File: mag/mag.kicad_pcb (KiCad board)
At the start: 2 copper layers, 96 x 41 mm, 28 parts, among them K1 кнопка_FSMSM, K2 кнопка_FSMSM

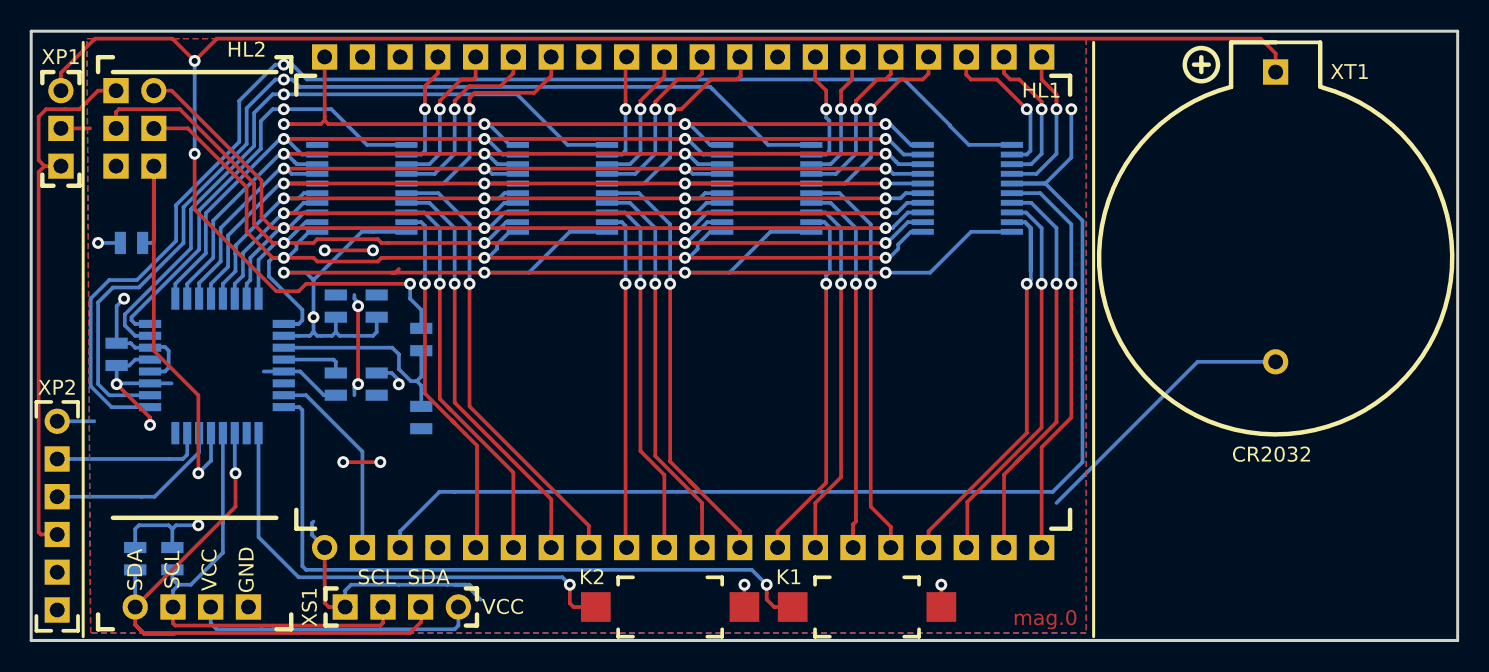
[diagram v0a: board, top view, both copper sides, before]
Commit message: подготавливается переделка под стационарные датчики
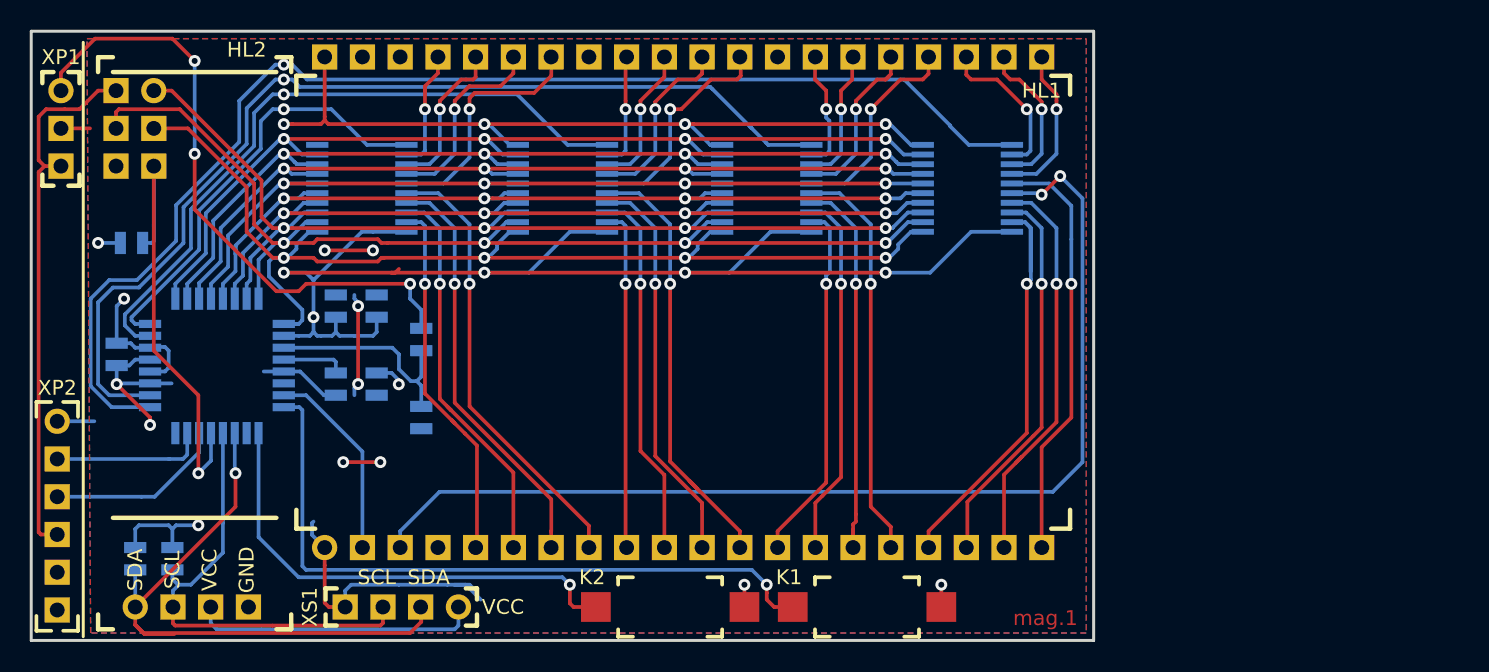
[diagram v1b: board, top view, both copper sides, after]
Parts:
- removed the G*** at (177.8, 61.0)
- removed the G*** at (188.2, 60.0)
- removed XТ1: Клеммник_х2, N_X:батарейный_отсек_CR2032
- added G***: LOGO, N_ICO:instagram_3x3, B.Cu at (120.0, 30.0)
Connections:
- net /PC3 renamed Net-(DD1-Pad26)
- HL1 pad 20: /Out44 -> /Out45
- HL1 pad 3: /Out45 -> /Out44
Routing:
- net /VCC_bat: track 117.1 -> 42.1 mm
- net /Out45: track 79.2 -> 28.4 mm
- net /Out44: track 27.7 -> 72.6 mm, vias 1 -> 2
- net /GND: track 127.7 -> 109.0 mm
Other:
- board size 96 x 41 mm -> 71.5 x 41 mm
- board text added: "el.a.nikitos"
- board text added: "mag.1"
- board text removed: "CR2032"
- board text removed: "mag.0"

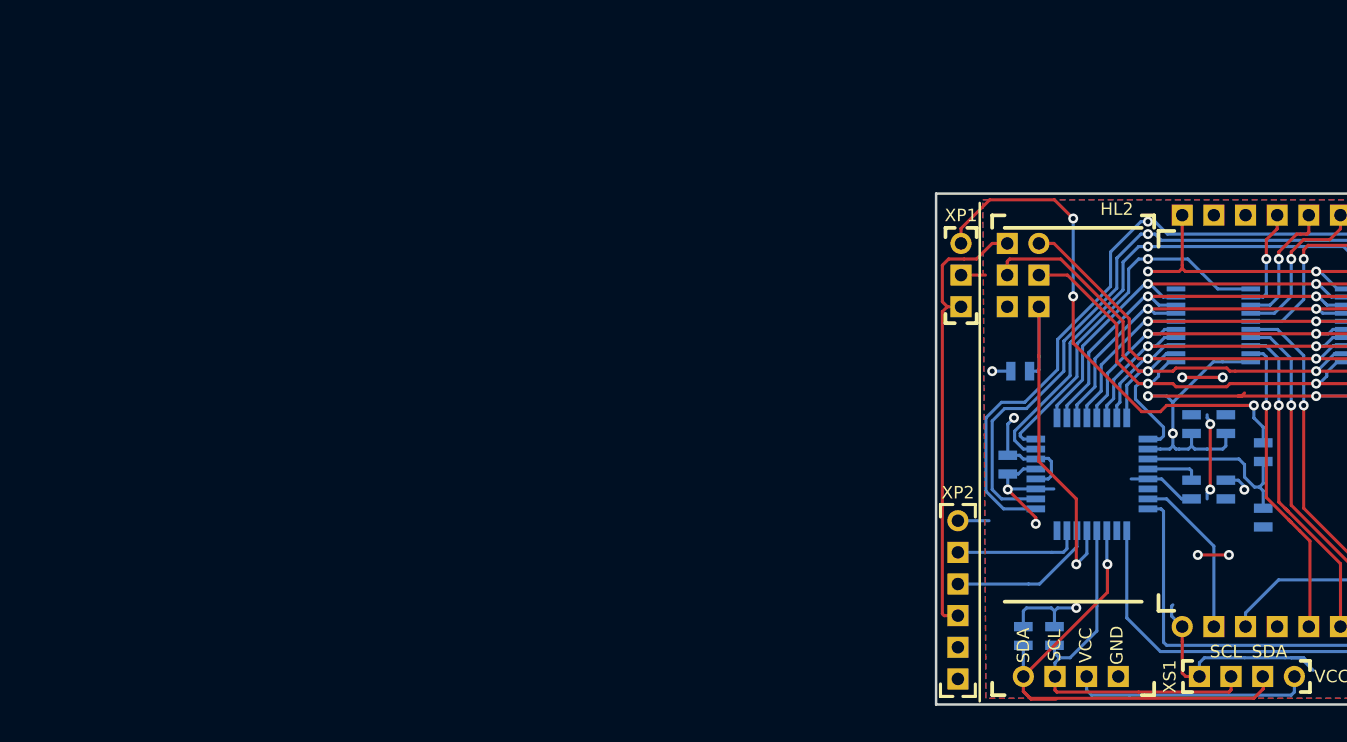
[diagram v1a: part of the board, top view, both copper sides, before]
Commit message: выложена схема питания и преобразователя
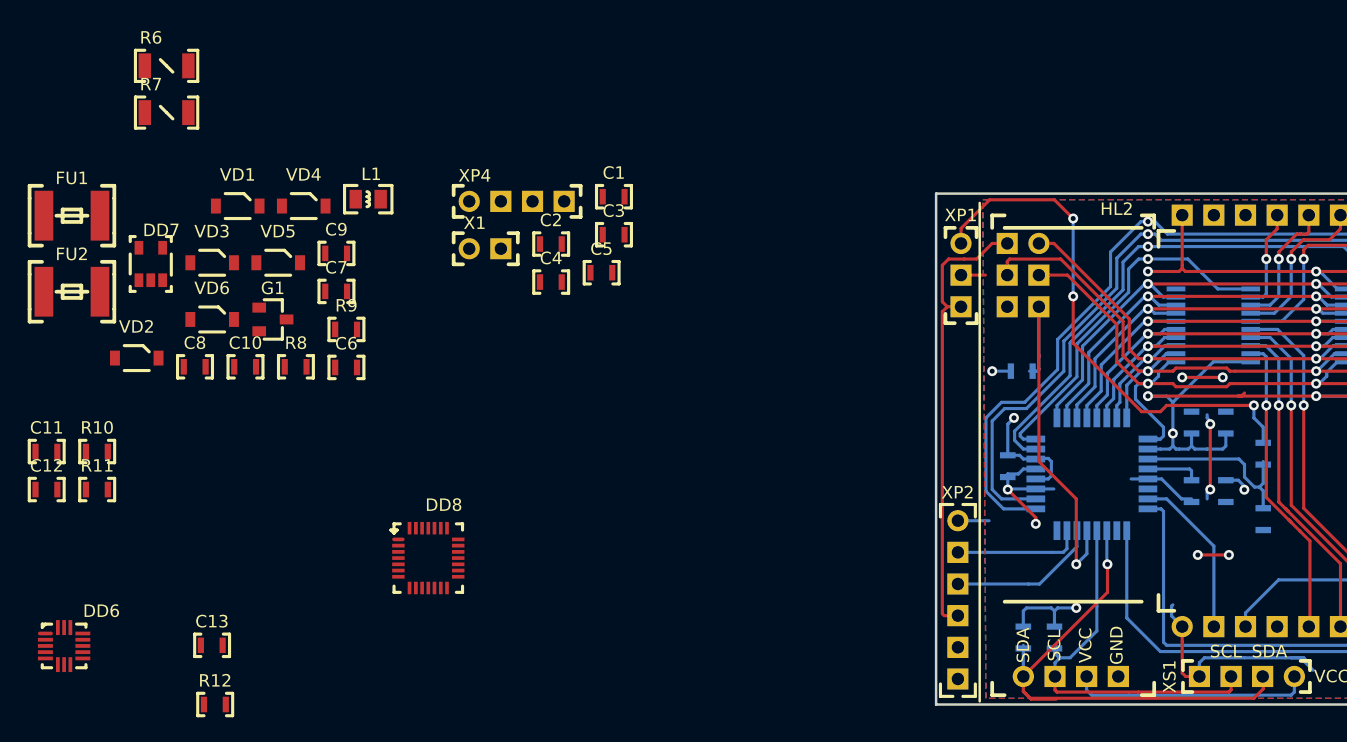
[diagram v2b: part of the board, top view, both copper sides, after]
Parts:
- added C1: Конденсатор_керамический, N_RLC:Конденсатор_SMD_0603, F.Cu at (71.2, 40.5)
- added C10: Конденсатор_керамический, N_RLC:Конденсатор_SMD_0603, F.Cu at (41.7, 54.1)
- added C11: Конденсатор_керамический, N_RLC:Конденсатор_SMD_0603, F.Cu at (25.7, 61.0)
- added C12: Конденсатор_керамический, N_RLC:Конденсатор_SMD_0603, F.Cu at (25.7, 64.0)
- added C13: Конденсатор_керамический, N_RLC:Конденсатор_SMD_0603, F.Cu at (39.0, 76.5)
- added C2: Конденсатор_керамический, N_RLC:Конденсатор_SMD_0603, F.Cu at (66.2, 44.3)
- added C3: Конденсатор_керамический, N_RLC:Конденсатор_SMD_0603, F.Cu at (71.2, 43.5)
- added C4: Конденсатор_керамический, N_RLC:Конденсатор_SMD_0603, F.Cu at (66.2, 47.4)
- added C5: Конденсатор_керамический, N_RLC:Конденсатор_SMD_0603, F.Cu at (70.3, 46.6)
- added C6: Конденсатор_керамический, N_RLC:Конденсатор_SMD_0603, F.Cu at (49.8, 54.2)
- added C7: Конденсатор_керамический, N_RLC:Конденсатор_SMD_0603, F.Cu at (49.0, 48.1)
- added C8: Конденсатор_керамический, N_RLC:Конденсатор_SMD_0603, F.Cu at (37.6, 54.1)
- added C9: Конденсатор_керамический, N_RLC:Конденсатор_SMD_0603, F.Cu at (49.0, 45.0)
- added DD6: LIS3DH, N_DD:акселерометр_LIS3DH, F.Cu at (28.0, 76.5)
- added DD7: Микросхема_DCDC_step_UP_TPS61040, N_G:Преобразователь_LM2703_SOT-23-5, F.Cu at (34.0, 47.2)
- added DD8: Преобразователь_CP2102(USB-UART), N_DD:Микросхема_CP2102, F.Cu at (54.8, 67.0)
- added FU1: Предохранитель_MF-MSMF010, N_RLC:Предохранитель_SMD_1812, F.Cu at (26.4, 42.0)
- added FU2: Предохранитель_MF-MSMF010, N_RLC:Предохранитель_SMD_1812, F.Cu at (26.4, 48.1)
- added G1: стабилизатор_XC6206P302MR, N_VD_HL:Транзистор_IRLML6344TR_SOT-23, F.Cu at (44.8, 50.4)
- added L1: Чип-индуктивность, N_RLC:Чип-индуктивность_SMD_0805, F.Cu at (51.4, 40.7)
- added R10: Резистор_0,065Вт, N_RLC:Конденсатор_SMD_0603, F.Cu at (29.8, 61.0)
- added R11: Резистор_0,065Вт, N_RLC:Конденсатор_SMD_0603, F.Cu at (29.8, 64.0)
- added R12: Резистор_0,065Вт, N_RLC:Конденсатор_SMD_0603, F.Cu at (39.2, 81.2)
- added R6: Резистор_0,25Вт, N_RLC:Резистор_SMD_1206-0,25_Вт, F.Cu at (34.5, 30.0)
- added R7: Резистор_0,25Вт, N_RLC:Резистор_SMD_1206-0,25_Вт, F.Cu at (34.5, 33.8)
- added R8: Резистор_0,065Вт, N_RLC:Конденсатор_SMD_0603, F.Cu at (45.7, 54.1)
- added R9: Резистор_0,065Вт, N_RLC:Конденсатор_SMD_0603, F.Cu at (49.8, 51.1)
- added VD1: Диод_S13, N_VD_HL:Диод_S13_SOD-123, F.Cu at (42.0, 41.2)
- added VD2: Диод_S13, N_VD_HL:Диод_S13_SOD-123, F.Cu at (33.9, 53.5)
- added VD3: Диод_S13, N_VD_HL:Диод_S13_SOD-123, F.Cu at (39.9, 45.8)
- added VD4: Диод_S13, N_VD_HL:Диод_S13_SOD-123, F.Cu at (47.3, 41.2)
- added VD5: Диод_S13, N_VD_HL:Диод_S13_SOD-123, F.Cu at (45.2, 45.8)
- added VD6: Диод_S13, N_VD_HL:Диод_S13_SOD-123, F.Cu at (39.9, 50.4)
- added X1: Клеммник_х2, N_X:Вилка_PLS2_вертикальная, F.Cu at (60.5, 44.7)
- added XP4: USB_female, N_X:Вилка_PLS4_вертикальная, F.Cu at (60.5, 40.9)
- DD1: value ATmega8A-AU -> ATmega328
- R1, R2, R3, R4, R5: value 20k_0603 -> Резистор_0,065Вт
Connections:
- R4 pad 1: /VCC_bat -> Net-(R4-Pad1)
- R4 pad 2: /ADC6 -> Net-(R4-Pad2)
- R5 pad 1: /ADC6 -> Net-(R5-Pad1)
- R5 pad 2: /GND -> Net-(R5-Pad2)
